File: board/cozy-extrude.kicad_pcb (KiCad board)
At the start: 2 copper layers, 8 parts, among them J1 RPi-Pico-Socket, J2 BME280, J3 PWM-Fan, J4 Screw_Terminal_01x02, J5 Screw_Terminal_01x02, K1 HF46F_5-HS1, U1 ULN2003

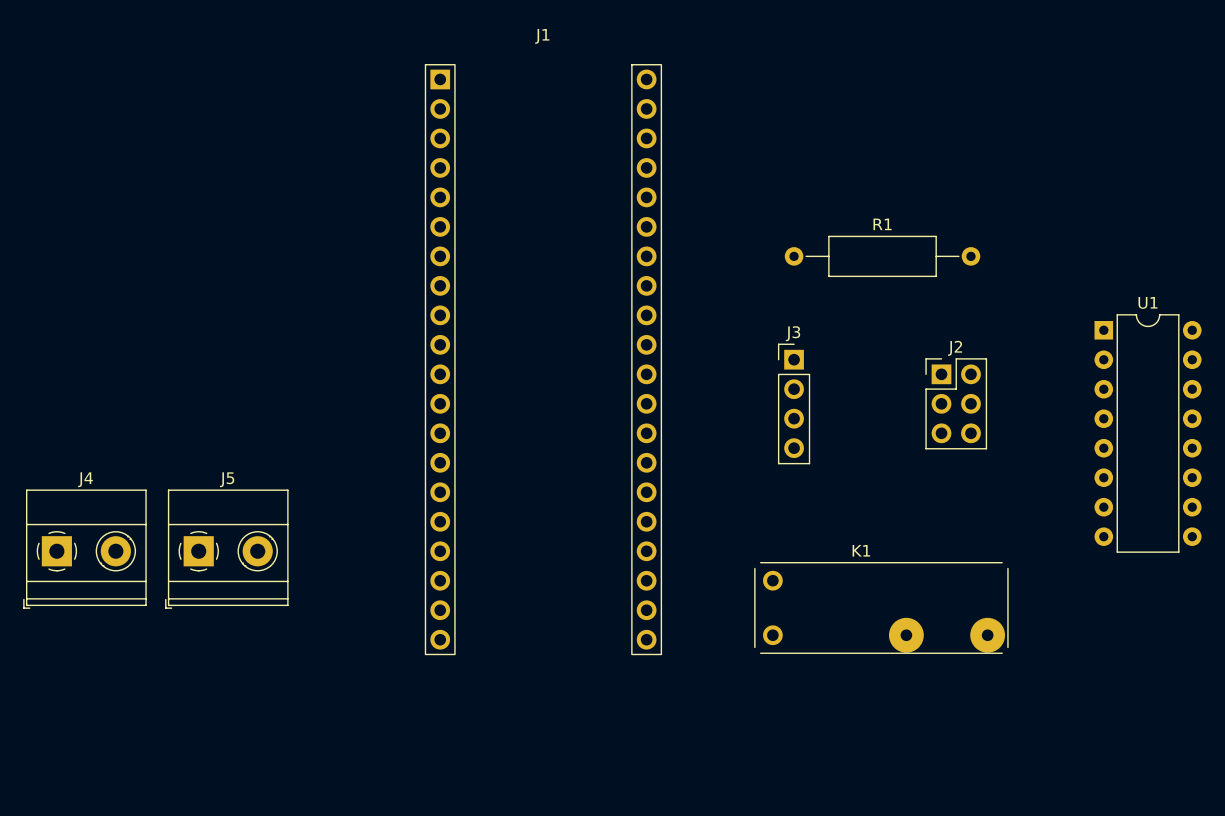
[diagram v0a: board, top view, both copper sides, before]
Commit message: import current footprints
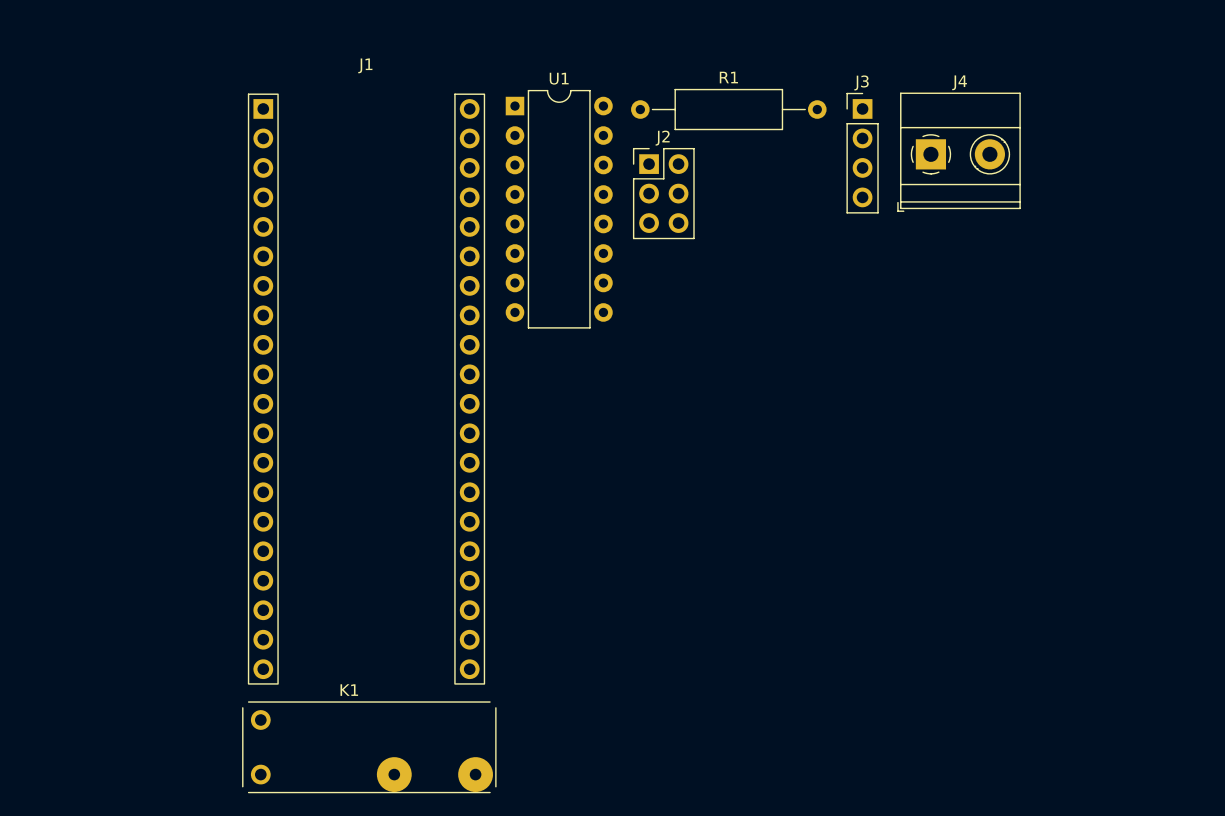
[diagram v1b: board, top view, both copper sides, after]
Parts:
- removed J5: Screw_Terminal_01x02, TerminalBlock_Phoenix:TerminalBlock_Phoenix_MKDS-1,5-2-5.08_1x02_P5.08mm_Horizontal
- J4: value Screw_Terminal_01x02 -> Heater-Switch
- moved J4 82.7 mm to (136.2, 57.2)
- moved U1 54.3 mm to (100.4, 53.1)
- moved K1 45.7 mm to (78.5, 106.0)
- moved J2 31.0 mm to (112.0, 58.1)
- moved J3 22.4 mm to (130.4, 53.3)
- moved R1 18.3 mm to (111.2, 53.4)
- moved J1 15.5 mm to (78.7, 53.3)
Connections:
- J1 pad 20: unconnected-(J1-Pad20) -> /TACH
- J1 pad 21: unconnected-(J1-Pad21) -> /SDO
- J1 pad 22: unconnected-(J1-Pad22) -> /CSB
- J1 pad 24: unconnected-(J1-Pad24) -> /SCL
- J1 pad 25: unconnected-(J1-Pad25) -> /SDA
- J1 pad 29: unconnected-(J1-Pad29) -> /HEATER_EN
- J1 pad 3: unconnected-(J1-Pad3) -> GND
- J1 pad 36: unconnected-(J1-Pad36) -> +3V3
- J1 pad 38: unconnected-(J1-Pad38) -> GND
- J1 pad 4: unconnected-(J1-Pad4) -> /PWM
- J1 pad 40: unconnected-(J1-Pad40) -> VBUS
- J2 pad 1: unconnected-(J2-Pad1) -> GND
- J2 pad 2: unconnected-(J2-Pad2) -> +3V3
- J2 pad 3: unconnected-(J2-Pad3) -> /SDO
- J2 pad 4: unconnected-(J2-Pad4) -> /CSB
- J2 pad 5: unconnected-(J2-Pad5) -> /SCL
- J2 pad 6: unconnected-(J2-Pad6) -> /SDA
- J3 pad 1: unconnected-(J3-Pad1) -> GND
- J3 pad 2: unconnected-(J3-Pad2) -> VBUS
- J3 pad 3: unconnected-(J3-Pad3) -> /TACH
- J3 pad 4: unconnected-(J3-Pad4) -> /PWM
- J4 pad 1: unconnected-(J4-Pad1) -> Net-(J4-Pad1)
- J4 pad 2: unconnected-(J4-Pad2) -> Net-(J4-Pad2)
- K1 pad 1: unconnected-(K1-Pad1) -> Net-(K1-Pad1)
- K1 pad 2: unconnected-(K1-Pad2) -> +3.3V
- K1 pad 3: unconnected-(K1-Pad3) -> Net-(J4-Pad1)
- K1 pad 4: unconnected-(K1-Pad4) -> Net-(J4-Pad2)
- R1 pad 1: unconnected-(R1-Pad1) -> /TACH
- R1 pad 2: unconnected-(R1-Pad2) -> +3V3
- U1 pad 1: unconnected-(U1-Pad1) -> /HEATER_EN
- U1 pad 16: unconnected-(U1-Pad16) -> Net-(K1-Pad1)
- U1 pad 8: unconnected-(U1-Pad8) -> GND
- U1 pad 9: unconnected-(U1-Pad9) -> +3.3V

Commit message: pcb draft
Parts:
- added Mount: MountingHole_3.2mm_M3, MountingHole:MountingHole_3.2mm_M3, F.Cu at (113.0, 128.3)
- added Mount: MountingHole_3.2mm_M3, MountingHole:MountingHole_3.2mm_M3, F.Cu at (148.6, 128.3)
- added Mount: MountingHole_3.2mm_M3, MountingHole:MountingHole_3.2mm_M3, F.Cu at (148.6, 66.0)
- added Mount: MountingHole_3.2mm_M3, MountingHole:MountingHole_3.2mm_M3, F.Cu at (113.0, 66.0)
- J2: footprint Connector_PinHeader_2.54mm:PinHeader_2x03_P2.54mm_Vertical -> Connector_PinHeader_2.54mm:PinHeader_1x06_P2.54mm_Vertical
- J3: footprint Connector_PinHeader_2.54mm:PinHeader_1x04_P2.54mm_Vertical -> Connector_Molex:Molex_KK-254_AE-6410-04A_1x04_P2.54mm_Vertical
- moved J2 71.2 mm to (143.6, 121.9), turned to 180 degrees
- moved J3 70.7 mm to (113.0, 121.9), turned to 90 degrees
- moved R1 65.7 mm to (128.3, 116.8), turned to 90 degrees
- moved K1 65.2 mm to (143.7, 103.3), turned to 90 degrees
- moved J1 45.4 mm to (119.4, 73.6)
- moved U1 33.3 mm to (124.5, 76.2)
- moved J4 23.7 mm to (146.4, 78.7), turned to 90 degrees
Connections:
- J1 pad 23: unconnected-(J1-Pad23) -> GND
- J1 pad 38: GND -> unconnected-(J1-Pad38)
- J4 pad 2: Net-(J4-Pad2) -> Net-(K1-Pad3)
- K1 pad 2: +3.3V -> +3V3
- K1 pad 3: Net-(J4-Pad1) -> Net-(K1-Pad3)
- K1 pad 4: Net-(J4-Pad2) -> Net-(J4-Pad1)
- U1 pad 9: +3.3V -> +3V3
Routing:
- net GND: track 0.00 -> 93.6 mm
- net +3V3: track 0.00 -> 74.4 mm
- net VBUS: track 0.00 -> 73.7 mm, vias 0 -> 2
- net Net-(K1-Pad1): track 0.00 -> 52.0 mm
- net /HEATER_EN: track 0.00 -> 48.1 mm
- net /PWM: track 0.00 -> 35.7 mm
- net Net-(K1-Pad3): track 0.00 -> 23.4 mm
- net /TACH: track 0.00 -> 21.7 mm
- net /CSB: track 0.00 -> 10.0 mm
- net /SDO: track 0.00 -> 9.49 mm
- net /SCL: track 0.00 -> 7.46 mm
- net /SDA: track 0.00 -> 7.46 mm
- net Net-(J4-Pad1): track 0.00 -> 6.98 mm
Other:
- board outline added: 43.2 x 69.9 mm

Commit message: make power net 2mm
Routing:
- net Net-(J4-Pad2): track 23.4 -> 25.3 mm
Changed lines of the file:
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@@
   (net 52 "unconnected-(J1-Pad18)")
   (net 53 "unconnected-(J1-Pad38)")
-  (net 54 "Net-(K1-Pad3)")
+  (net 54 "Net-(J4-Pad2)")
   (footprint "TerminalBlock_Phoenix:TerminalBlock_Phoenix_MKDS-1,5-2-5.08_1x02_P5.08mm_Horizontal" (layer "F.Cu")
     (at 146.406958 78.706852 90)
@@
       (net 38 "Net-(J4-Pad1)") (pinfunction "Pin_1") (pintype "passive"))
     (pad "2" thru_hole circle (at 5.08 0 90) (size 2.6 2.6) (drill 1.3) (layers *.Cu *.Mask)
-      (net 54 "Net-(K1-Pad3)") (pinfunction "Pin_2") (pintype "passive"))
+      (net 54 "Net-(J4-Pad2)") (pinfunction "Pin_2") (pintype "passive"))
     (model "${KICAD6_3DMODEL_DIR}/TerminalBlock_Phoenix.3dshapes/TerminalBlock_Phoenix_MKDS-1,5-2-5.08_1x02_P5.08mm_Horizontal.wrl"
       (offset (xyz 0 0 0))
@@
     (fp_line (start -1.05 6.25) (end 19.75 6.25) (layer "F.SilkS") (width 0.12))
     (fp_line (start -1.55 -1.05) (end -1.55 5.75) (layer "F.SilkS") (width 0.12))
+    (fp_line (start -1.05 -1.05) (end -1.05 5.75) (layer "F.CrtYd") (width 0.12))
+    (fp_line (start -1.05 5.75) (end 19.75 5.75) (layer "F.CrtYd") (width 0.12))
     (fp_line (start -1.05 -1.05) (end 19.75 -1.05) (layer "F.CrtYd") (width 0.12))
     (fp_line (start 19.75 -1.05) (end 19.75 5.75) (layer "F.CrtYd") (width 0.12))
-    (fp_line (start -1.05 -1.05) (end -1.05 5.75) (layer "F.CrtYd") (width 0.12))
-    (fp_line (start -1.05 5.75) (end 19.75 5.75) (layer "F.CrtYd") (width 0.12))
     (pad "1" thru_hole circle (at 0 0 90) (size 1.7 1.7) (drill 1) (layers *.Cu *.Mask)
       (net 39 "Net-(K1-Pad1)") (pintype "passive"))
     (pad "2" thru_hole circle (at 0 4.7 90) (size 1.7 1.7) (drill 1) (layers *.Cu *.Mask)
       (net 34 "+3V3") (pintype "passive"))
-    (pad "3" thru_hole circle (at 11.5 4.7 90) (size 3 3) (drill 1) (layers *.Cu *.Mask)
-      (net 54 "Net-(K1-Pad3)") (pintype "passive"))
-    (pad "4" thru_hole circle (at 18.5 4.7 90) (size 3 3) (drill 1) (layers *.Cu *.Mask)
+    (pad "3" thru_hole circle (at 11.5 4.7 90) (size 2 2) (drill 1) (layers *.Cu *.Mask)
+      (net 54 "Net-(J4-Pad2)") (pintype "passive"))
+    (pad "4" thru_hole circle (at 18.5 4.7 90) (size 2 2) (drill 1) (layers *.Cu *.Mask)
       (net 38 "Net-(J4-Pad1)") (pintype "passive"))
     (model "${KIPRJMOD}/lib/HF46F.step"
@@
   (segment (start 133.35 71.081852) (end 134.62 71.081852) (width 1) (layer "B.Cu") (net 36))
   (segment (start 148.4 84.791852) (end 148.33 84.791852) (width 1) (layer "B.Cu") (net 38))
-  (segment (start 148.4 84.791852) (end 148.4 80.699894) (width 3) (layer "B.Cu") (net 38))
-  (segment (start 148.4 80.699894) (end 146.406958 78.706852) (width 3) (layer "B.Cu") (net 38))
+  (segment (start 148.4 80.699894) (end 146.406958 78.706852) (width 2) (layer "B.Cu") (net 38))
+  (segment (start 148.4 84.791852) (end 148.4 80.699894) (width 2) (layer "B.Cu") (net 38))
   (segment (start 135.89 68.541852) (end 132.08 68.541852) (width 1) (layer "B.Cu") (net 39))
   (segment (start 132.08 74.891852) (end 132.08 76.161852) (width 1) (layer "B.Cu") (net 39))
@@
   (segment (start 141.2 100.791852) (end 141.2 84.011852) (width 1) (layer "B.Cu") (net 39))
   (segment (start 141.2 84.011852) (end 139.7 82.511852) (width 1) (layer "B.Cu") (net 39))
-  (segment (start 148.4 91.791852) (end 144.78 88.171852) (width 3) (layer "B.Cu") (net 54))
-  (segment (start 144.78 88.171852) (end 144.78 82.511852) (width 3) (layer "B.Cu") (net 54))
-  (segment (start 142.24 79.971852) (end 142.24 76.161852) (width 3) (layer "B.Cu") (net 54))
-  (segment (start 144.775 73.626852) (end 146.406958 73.626852) (width 3) (layer "B.Cu") (net 54))
-  (segment (start 144.78 82.511852) (end 142.24 79.971852) (width 3) (layer "B.Cu") (net 54))
-  (segment (start 142.24 76.161852) (end 144.775 73.626852) (width 3) (layer "B.Cu") (net 54))
+  (segment (start 144.78 82.55) (end 142.24 80.01) (width 2) (layer "B.Cu") (net 54))
+  (segment (start 142.24 74.93) (end 143.543148 73.626852) (width 2) (layer "B.Cu") (net 54))
+  (segment (start 148.4 91.791852) (end 146.401852 91.791852) (width 2) (layer "B.Cu") (net 54))
+  (segment (start 146.401852 91.791852) (end 144.78 90.17) (width 2) (layer "B.Cu") (net 54))
+  (segment (start 144.78 90.17) (end 144.78 82.55) (width 2) (layer "B.Cu") (net 54))
+  (segment (start 143.543148 73.626852) (end 146.406958 73.626852) (width 2) (layer "B.Cu") (net 54))
+  (segment (start 142.24 80.01) (end 142.24 74.93) (width 2) (layer "B.Cu") (net 54))
 )

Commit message: improved hf46f footprint and model
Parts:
- K1: footprint Hongfa-HF46F:HF46F_5-HS1 -> Hongfa-HF46F:HF46F
- moved K1 0.42 mm to (143.7, 102.9)
- moved J4 0.36 mm to (146.1, 78.7)
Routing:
- net Net-(J4-Pad2): track 25.3 -> 23.7 mm
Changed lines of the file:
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@@
     (pad_to_mask_clearance 0)
     (pcbplotparams
-      (layerselection 0x00010fc_ffffffff)
+      (layerselection 0x0001020_ffffffff)
       (disableapertmacros false)
       (usegerberextensions false)
@@
       (outputformat 1)
       (mirror false)
-      (drillshape 1)
+      (drillshape 0)
       (scaleselection 1)
       (outputdirectory "")
@@
   (net 54 "Net-(J4-Pad2)")
   (footprint "TerminalBlock_Phoenix:TerminalBlock_Phoenix_MKDS-1,5-2-5.08_1x02_P5.08mm_Horizontal" (layer "F.Cu")
-    (at 146.406958 78.706852 90)
+    (at 146.05 78.740041 90)
     (descr "Terminal Block Phoenix MKDS-1,5-2-5.08, 2 pins, pitch 5.08mm, size 10.2x9.8mm^2, drill diamater 1.3mm, pad diameter 2.6mm, see http://www.farnell.com/datasheets/100425.pdf, script-generated using https://github.com/pointhi/kicad-footprint-generator/scripts/TerminalBlock_Phoenix")
     (tags "THT Terminal Block Phoenix MKDS-1,5-2-5.08 pitch 5.08mm size 10.2x9.8mm^2 drill 1.3mm pad 2.6mm")
@@
     )
   )
-  (footprint "Hongfa-HF46F:HF46F_5-HS1" (layer "F.Cu")
-    (at 143.7 103.291852 90)
+  (footprint "Hongfa-HF46F:HF46F" (layer "F.Cu")
+    (at 143.7 102.87 90)
     (property "Sheetfile" "cozy-extrude.kicad_sch")
     (property "Sheetname" "")
@@
       (effects (font (size 1 1) (thickness 0.15)))
     )
-    (fp_line (start -1.05 -1.55) (end 19.75 -1.55) (layer "F.SilkS") (width 0.12))
-    (fp_line (start 20.25 -1.05) (end 20.25 5.75) (layer "F.SilkS") (width 0.12))
-    (fp_line (start -1.05 6.25) (end 19.75 6.25) (layer "F.SilkS") (width 0.12))
-    (fp_line (start -1.55 -1.05) (end -1.55 5.75) (layer "F.SilkS") (width 0.12))
-    (fp_line (start -1.05 -1.05) (end -1.05 5.75) (layer "F.CrtYd") (width 0.12))
-    (fp_line (start -1.05 5.75) (end 19.75 5.75) (layer "F.CrtYd") (width 0.12))
+    (fp_line (start -1.55 -1.55) (end -1.55 6.25) (layer "F.SilkS") (width 0.12))
+    (fp_line (start -1.55 6.25) (end 20.25 6.25) (layer "F.SilkS") (width 0.12))
+    (fp_line (start -1.55 -1.55) (end 20.25 -1.55) (layer "F.SilkS") (width 0.12))
+    (fp_line (start 20.25 -1.55) (end 20.25 6.25) (layer "F.SilkS") (width 0.12))
     (fp_line (start -1.05 -1.05) (end 19.75 -1.05) (layer "F.CrtYd") (width 0.12))
     (fp_line (start 19.75 -1.05) (end 19.75 5.75) (layer "F.CrtYd") (width 0.12))
-    (pad "1" thru_hole circle (at 0 0 90) (size 1.7 1.7) (drill 1) (layers *.Cu *.Mask)
+    (fp_line (start -1.05 5.75) (end 19.75 5.75) (layer "F.CrtYd") (width 0.12))
+    (fp_line (start -1.05 -1.05) (end -1.05 5.75) (layer "F.CrtYd") (width 0.12))
+    (pad "1" thru_hole circle (at 0 0 90) (size 1.7 1.7) (drill 0.8) (layers *.Cu *.Mask)
       (net 39 "Net-(K1-Pad1)") (pintype "passive"))
-    (pad "2" thru_hole circle (at 0 4.7 90) (size 1.7 1.7) (drill 1) (layers *.Cu *.Mask)
+    (pad "2" thru_hole circle (at 0 4.7 90) (size 1.7 1.7) (drill 0.8) (layers *.Cu *.Mask)
       (net 34 "+3V3") (pintype "passive"))
-    (pad "3" thru_hole circle (at 11.5 4.7 90) (size 2 2) (drill 1) (layers *.Cu *.Mask)
+    (pad "3" thru_hole circle (at 11.5 4.7 90) (size 1.8 1.8) (drill oval 0.8 1) (layers *.Cu *.Mask)
       (net 54 "Net-(J4-Pad2)") (pintype "passive"))
-    (pad "4" thru_hole circle (at 18.5 4.7 90) (size 2 2) (drill 1) (layers *.Cu *.Mask)
+    (pad "4" thru_hole circle (at 18.5 4.7 90) (size 1.8 1.8) (drill oval 0.8 1) (layers *.Cu *.Mask)
       (net 38 "Net-(J4-Pad1)") (pintype "passive"))
     (model "${KIPRJMOD}/lib/HF46F.step"
@@
     )
   )
-  (gr_rect (start 109.22 62.191852) (end 152.4 132.041852) (layer "Edge.Cuts") (width 0.1) (fill none))
+  (gr_rect (start 109.22 62.191885) (end 152.4 132.041885) (layer "Edge.Cuts") (width 0.1) (fill none))
   (segment (start 124.46 93.941852) (end 124.46 104.178148) (width 1) (layer "F.Cu") (net 3))
   (segment (start 137.083704 116.801852) (end 137.16 116.801852) (width 1) (layer "F.Cu") (net 3))
@@
   (segment (start 128.27 77.431852) (end 128.27 97.751852) (width 1) (layer "B.Cu") (net 27))
   (segment (start 132.08 105.371852) (end 134.62 102.831852) (width 1) (layer "B.Cu") (net 27))
+  (segment (start 146.05 105.22) (end 148.4 102.87) (width 1) (layer "B.Cu") (net 34))
   (segment (start 143.57 119.341852) (end 143.646296 119.341852) (width 1) (layer "B.Cu") (net 34))
   (segment (start 138.43 83.781852) (end 137.16 83.781852) (width 1) (layer "B.Cu") (net 34))
-  (segment (start 146.05 105.641852) (end 146.05 106.641852) (width 1) (layer "B.Cu") (net 34))
   (segment (start 133.35 93.941852) (end 134.62 92.671852) (width 1) (layer "B.Cu") (net 34))
   (segment (start 134.62 83.781852) (end 134.62 92.671852) (width 1) (layer "B.Cu") (net 34))
@@
   (segment (start 134.62 96.481852) (end 129.54 101.561852) (width 1) (layer "B.Cu") (net 34))
   (segment (start 142.24 106.641852) (end 146.05 106.641852) (width 1) (layer "B.Cu") (net 34))
-  (segment (start 148.4 103.291852) (end 146.05 105.641852) (width 1) (layer "B.Cu") (net 34))
   (segment (start 139.7 104.101852) (end 142.24 106.641852) (width 1) (layer "B.Cu") (net 34))
   (segment (start 132.08 93.941852) (end 133.35 93.941852) (width 1) (layer "B.Cu") (net 34))
   (segment (start 139.7 85.051852) (end 139.7 104.101852) (width 1) (layer "B.Cu") (net 34))
   (segment (start 143.646296 119.341852) (end 146.05 116.938148) (width 1) (layer "B.Cu") (net 34))
+  (segment (start 146.05 106.641852) (end 146.05 105.22) (width 1) (layer "B.Cu") (net 34))
   (segment (start 134.62 92.671852) (end 134.62 96.481852) (width 1) (layer "B.Cu") (net 34))
   (segment (start 139.7 85.051852) (end 138.43 83.781852) (width 1) (layer "B.Cu") (net 34))
@@
   (segment (start 113.05 119.341852) (end 111.76 119.341852) (width 1) (layer "B.Cu") (net 36))
   (segment (start 133.35 71.081852) (end 134.62 71.081852) (width 1) (layer "B.Cu") (net 36))
-  (segment (start 148.4 84.791852) (end 148.33 84.791852) (width 1) (layer "B.Cu") (net 38))
-  (segment (start 148.4 80.699894) (end 146.406958 78.706852) (width 2) (layer "B.Cu") (net 38))
-  (segment (start 148.4 84.791852) (end 148.4 80.699894) (width 2) (layer "B.Cu") (net 38))
+  (segment (start 146.050041 78.740041) (end 146.05 78.740041) (width 2) (layer "B.Cu") (net 38))
+  (segment (start 148.4 81.09) (end 146.050041 78.740041) (width 2) (layer "B.Cu") (net 38))
+  (segment (start 148.4 81.09) (end 148.4 84.37) (width 2) (layer "B.Cu") (net 38))
   (segment (start 135.89 68.541852) (end 132.08 68.541852) (width 1) (layer "B.Cu") (net 39))
+  (segment (start 141.2 100.37) (end 143.7 102.87) (width 1) (layer "B.Cu") (net 39))
   (segment (start 132.08 74.891852) (end 132.08 76.161852) (width 1) (layer "B.Cu") (net 39))
   (segment (start 132.08 68.541852) (end 130.81 69.811852) (width 1) (layer "B.Cu") (net 39))
-  (segment (start 143.7 103.291852) (end 141.2 100.791852) (width 1) (layer "B.Cu") (net 39))
   (segment (start 139.7 82.511852) (end 139.7 69.811852) (width 1) (layer "B.Cu") (net 39))
   (segment (start 139.7 69.811852) (end 137.16 69.811852) (width 1) (layer "B.Cu") (net 39))
   (segment (start 130.81 73.621852) (end 132.08 74.891852) (width 1) (layer "B.Cu") (net 39))
   (segment (start 137.16 69.811852) (end 135.89 68.541852) (width 1) (layer "B.Cu") (net 39))
+  (segment (start 141.2 84.011852) (end 141.2 100.37) (width 1) (layer "B.Cu") (net 39))
   (segment (start 130.81 69.811852) (end 130.81 73.621852) (width 1) (layer "B.Cu") (net 39))
-  (segment (start 141.2 100.791852) (end 141.2 84.011852) (width 1) (layer "B.Cu") (net 39))
   (segment (start 141.2 84.011852) (end 139.7 82.511852) (width 1) (layer "B.Cu") (net 39))
-  (segment (start 144.78 82.55) (end 142.24 80.01) (width 2) (layer "B.Cu") (net 54))
-  (segment (start 142.24 74.93) (end 143.543148 73.626852) (width 2) (layer "B.Cu") (net 54))
-  (segment (start 148.4 91.791852) (end 146.401852 91.791852) (width 2) (layer "B.Cu") (net 54))
-  (segment (start 146.401852 91.791852) (end 144.78 90.17) (width 2) (layer "B.Cu") (net 54))
-  (segment (start 144.78 90.17) (end 144.78 82.55) (width 2) (layer "B.Cu") (net 54))
-  (segment (start 143.543148 73.626852) (end 146.406958 73.626852) (width 2) (layer "B.Cu") (net 54))
-  (segment (start 142.24 80.01) (end 142.24 74.93) (width 2) (layer "B.Cu") (net 54))
+  (segment (start 143.543148 73.626852) (end 142.24 74.93) (width 2) (layer "B.Cu") (net 54))
+  (segment (start 146.406958 73.626852) (end 143.543148 73.626852) (width 2) (layer "B.Cu") (net 54))
+  (segment (start 142.24 74.93) (end 142.24 81.28) (width 2) (layer "B.Cu") (net 54))
+  (segment (start 144.78 83.82) (end 144.78 87.75) (width 2) (layer "B.Cu") (net 54))
+  (segment (start 142.24 81.28) (end 144.78 83.82) (width 2) (layer "B.Cu") (net 54))
+  (segment (start 144.78 87.75) (end 148.4 91.37) (width 2) (layer "B.Cu") (net 54))
 )
